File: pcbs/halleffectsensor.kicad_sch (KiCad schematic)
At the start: 2 parts, among them J2 Conn_01x04_Pin, U3 Si7210-B-xx-IV

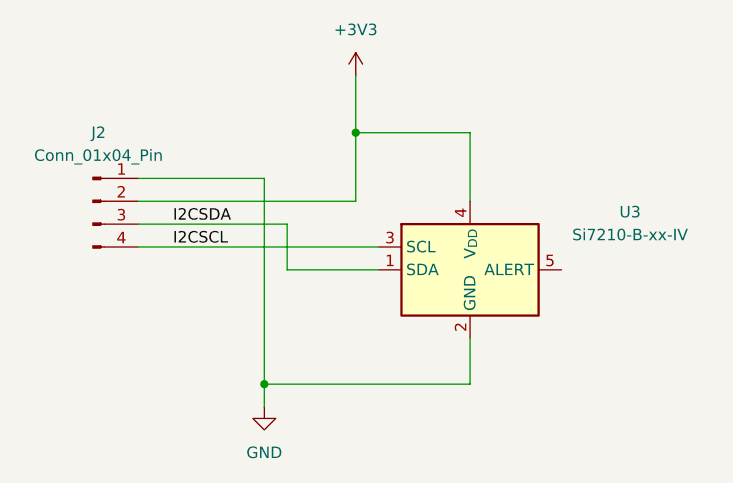
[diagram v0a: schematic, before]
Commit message: add ld2450, recreate simple hall effect sensor, add ssd1306 display
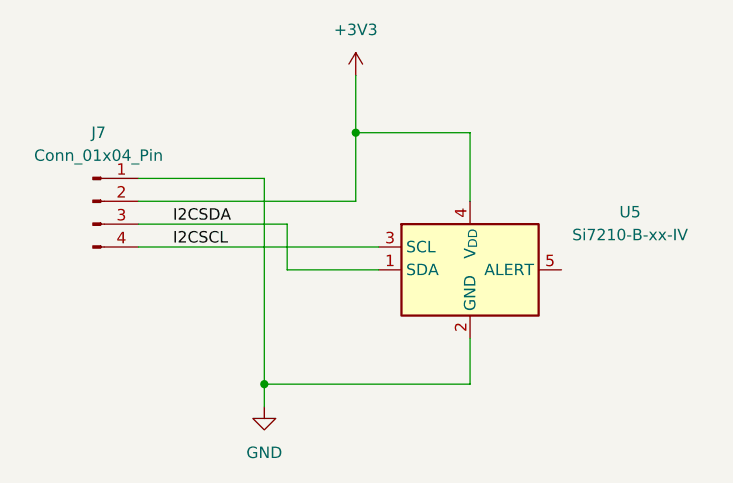
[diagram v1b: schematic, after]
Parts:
- renumbered J2 to J7, U3 to U5
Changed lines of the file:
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@@
 		(dnp no)
 		(fields_autoplaced yes)
-		(property "Reference" "#PWR09"
+		(property "Reference" "#PWR014"
 			(at 74.93 69.85 0)
 			(hide yes)
@@
 			(project "monstera"
 				(path "/f43ccbf1-dc73-4054-b062-aa68d83d24f7"
-					(reference "#PWR09")
+					(reference "#PWR014")
 					(unit 1)
 				)
@@
 		(in_pos_files yes)
 		(dnp no)
-		(property "Reference" "#PWR08"
+		(property "Reference" "#PWR015"
 			(at 85.09 30.48 0)
 			(hide yes)
@@
 			(project "monstera"
 				(path "/f43ccbf1-dc73-4054-b062-aa68d83d24f7"
-					(reference "#PWR08")
+					(reference "#PWR015")
 					(unit 1)
 				)
@@
 		(dnp no)
 		(fields_autoplaced yes)
-		(property "Reference" "U3"
+		(property "Reference" "U5"
 			(at 115.57 41.8398 0)
 			(show_name no)
@@
 			(project "monstera"
 				(path "/f43ccbf1-dc73-4054-b062-aa68d83d24f7"
-					(reference "U3")
+					(reference "U5")
 					(unit 1)
 				)
@@
 		(dnp no)
 		(fields_autoplaced yes)
-		(property "Reference" "J2"
+		(property "Reference" "J7"
 			(at 56.515 33.02 0)
 			(show_name no)
@@
 			(project "monstera"
 				(path "/f43ccbf1-dc73-4054-b062-aa68d83d24f7"
-					(reference "J2")
+					(reference "J7")
 					(unit 1)
 				)
